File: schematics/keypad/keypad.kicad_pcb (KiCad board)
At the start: 2 copper layers, 76.3 x 196.2 mm, 84 parts, among them J1 BOARD, J2 PRG, SW1 cherry_mx_rgb, SW10 cherry_mx_rgb, SW11 cherry_mx_rgb, SW12 cherry_mx_rgb, SW13 cherry_mx_rgb, SW14 cherry_mx_rgb, SW15 cherry_mx_rgb, SW16 cherry_mx_rgb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

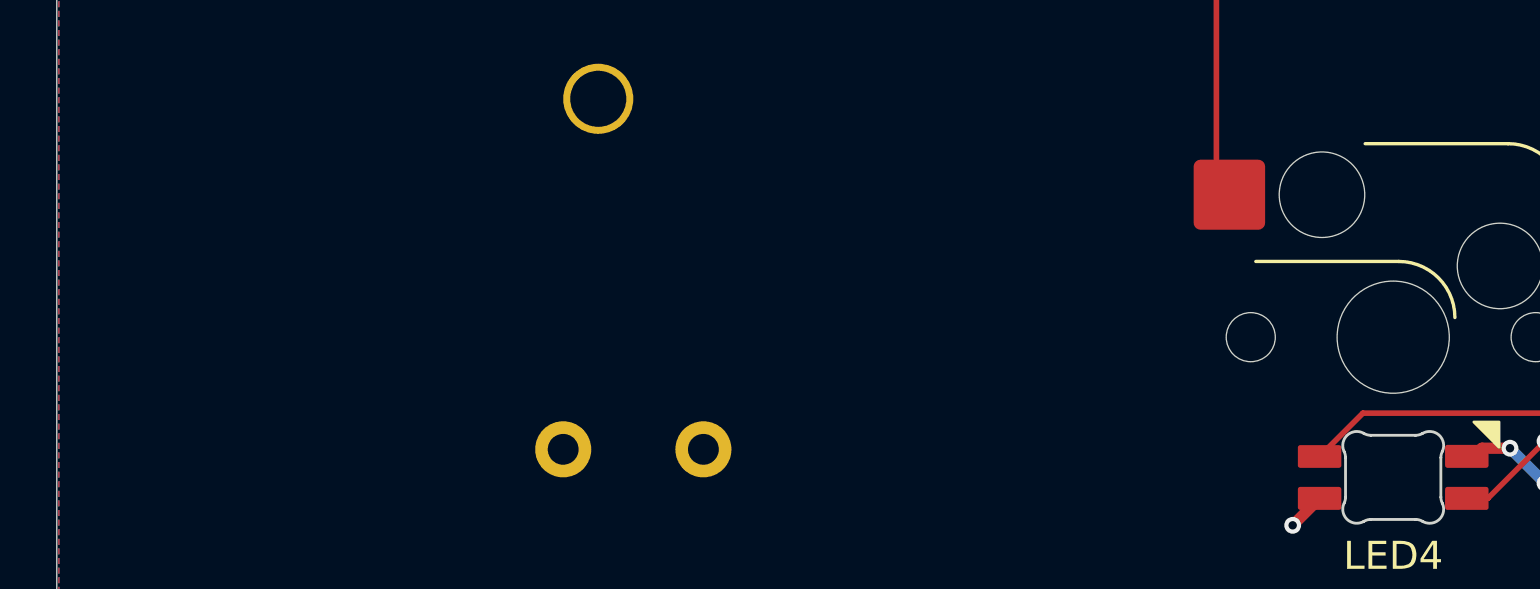
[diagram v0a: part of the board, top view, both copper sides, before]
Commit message: fix(hw): update keypad silkscreen
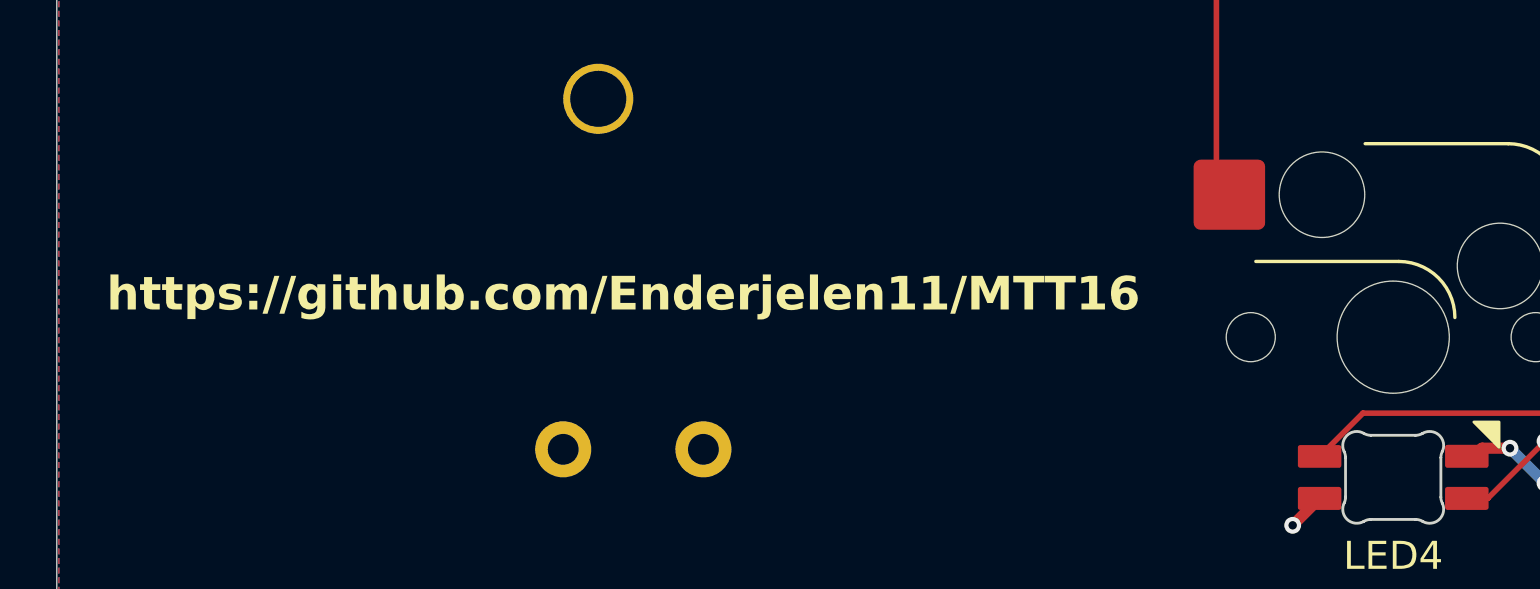
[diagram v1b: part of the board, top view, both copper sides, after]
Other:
- board text added: "https://github.com/Enderjelen11/MTT16"
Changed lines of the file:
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@@
+		)
+	)
+	(gr_text "https://github.com/Enderjelen11/MTT16"
+		(at 75.95 226.2 0)
+		(layer "F.SilkS")
+		(effects
+			(font
+				(size 1.2 1.2)
+				(thickness 0.2)
+				(bold yes)
+			)
+			(justify left bottom)
 		)
 	)

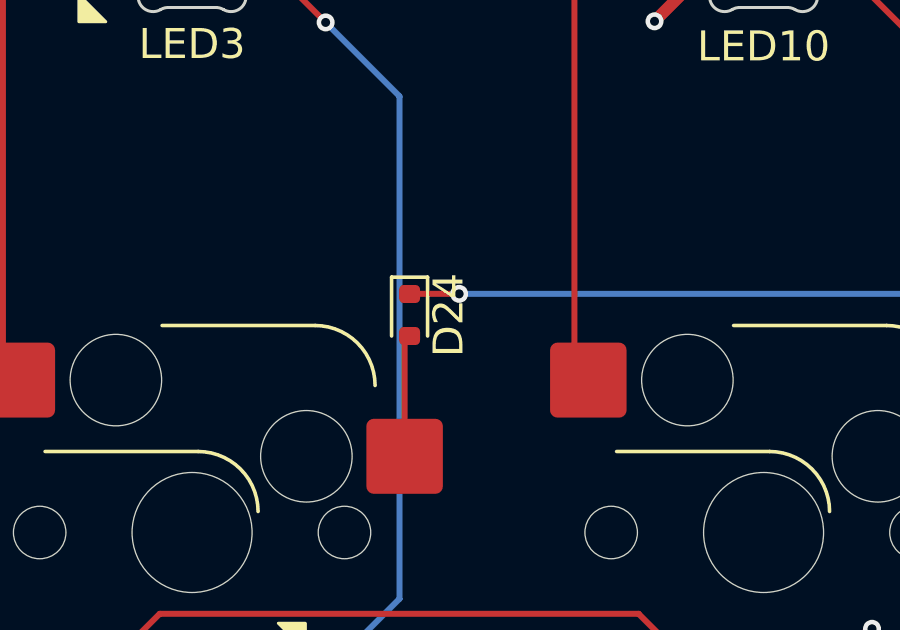
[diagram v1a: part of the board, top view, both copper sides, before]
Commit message: chore(hw): migrate keypad to KiCad v9
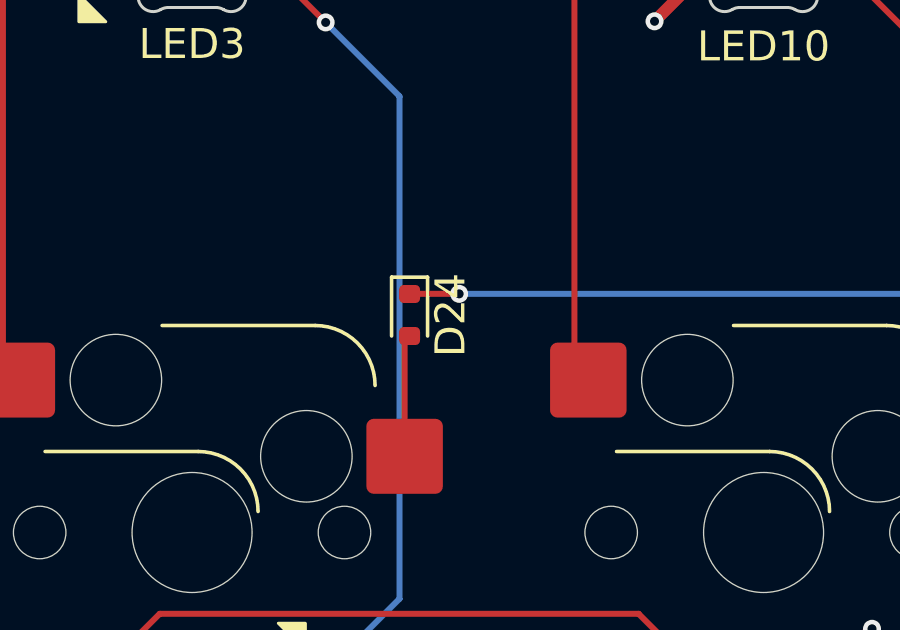
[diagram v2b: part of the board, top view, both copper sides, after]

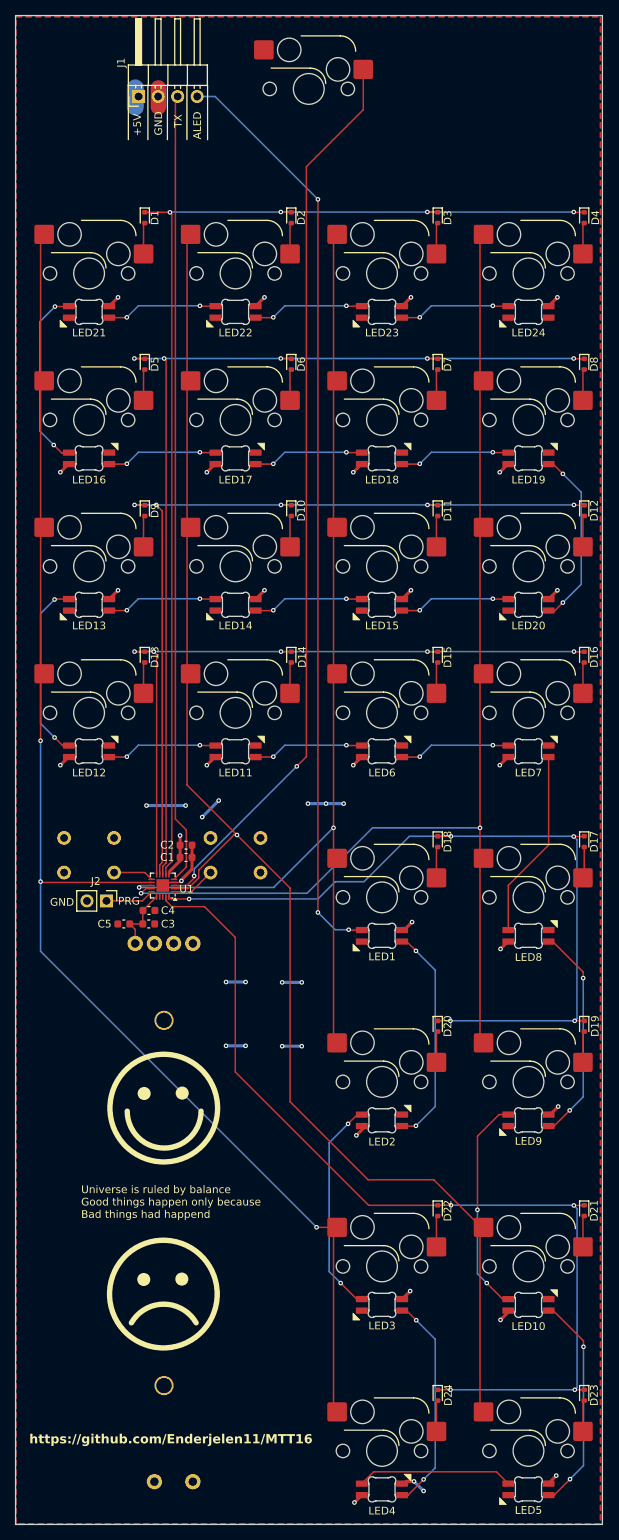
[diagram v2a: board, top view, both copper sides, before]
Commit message: hw: add encoder support to keypad
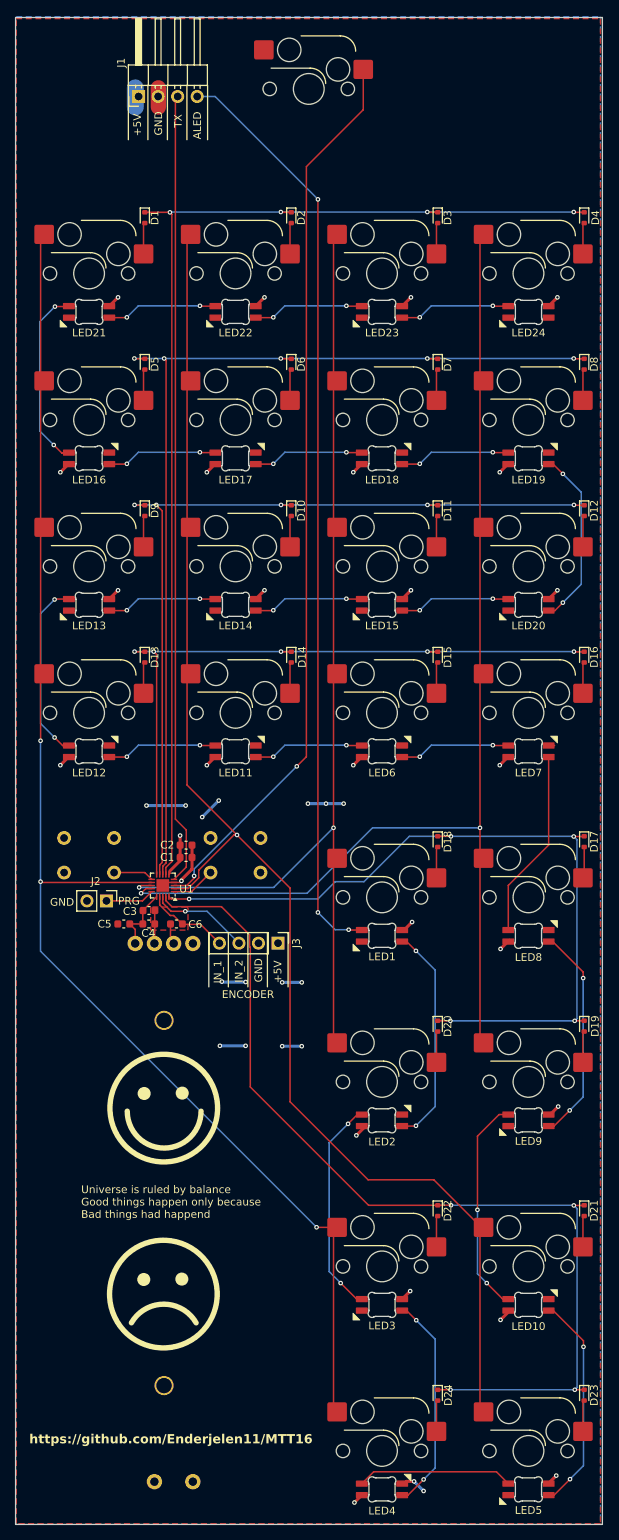
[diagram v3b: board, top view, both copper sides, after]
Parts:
- added C6: 0.1uF, Capacitor_SMD:C_0603_1608Metric, F.Cu at (95.1, 158.5)
- added J3: ENCODER, Connector_PinHeader_2.54mm:PinHeader_1x04_P2.54mm_Vertical, F.Cu at (108.3, 161.0)
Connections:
- U1 pad 17: unconnected-(U1-PD3-Pad17) -> /encoder
- U1 pad 18: unconnected-(U1-PD4-Pad18) -> /pd4
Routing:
- net /pd4: track 0.00 -> 12.9 mm, vias 0 -> 1
- net /encoder: track 0.00 -> 10.9 mm
- net GND: track 37.9 -> 46.3 mm
- net /km_r5: track 124.8 -> 126.1 mm
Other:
- board size 76.3 x 196.2 mm -> 76.3 x 196 mm
- board text added: "ENCODER"
- board text added: "IN_1"
- board text added: "IN_2"
